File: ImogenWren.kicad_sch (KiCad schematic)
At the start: 16 parts, among them J1 Battery Cell 4.2v, J3 WS2821b-LED-Out, SW1 SW_SPDT_small, U1 MCP73831-2-OT

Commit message: dfhdyhdre
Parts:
- J3: value WS2821b-LED-Out -> WS2821b; PIN1 (none) -> gnd; PIN1_NAME D -> (none); PIN2 (none) -> V+; PIN2_NAME V+ -> (none); PIN3 (none) -> D; PIN3_NAME G -> (none)
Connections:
- net GND: now also J3.A1; no longer J3.A3
- net at JP3.2 (C): now also J3.A3; no longer J3.A1
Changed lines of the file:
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@@
     )
   )
-  (symbol (lib_id "000-edge-connectors-immo:3-pin-edge-touch") (at 259.08 92.71 0) (unit 1)
+  (symbol (lib_id "000-edge-connectors-immo:3-pin-edge-touch") (at 260.35 80.01 0) (mirror x) (unit 1)
     (in_bom yes) (on_board yes) (dnp no)
-    (property "Reference" "J3" (at 255.905 72.39 0)
+    (property "Reference" "J3" (at 250.19 87.63 0)
       (effects (font (size 1.27 1.27)) (justify left))
     )
-    (property "Value" "WS2821b-LED-Out" (at 255.27 74.295 0)
+    (property "Value" "WS2821b" (at 249.555 85.725 0)
       (effects (font (size 1.27 1.27)) (justify left))
     )
-    (property "Footprint" "000-edge-connectors-immo:3-pin-edge" (at 243.84 132.08 0)
+    (property "Footprint" "000-edge-connectors-immo:3-pin-edge" (at 297.18 86.36 0)
       (effects (font (size 1.27 1.27)) hide)
     )
-    (property "Datasheet" "http://www.ritrontek.com/uploadfile/2016/1026/20161026105231124.pdf#page=63" (at 262.89 120.65 0)
+    (property "Datasheet" "http://www.ritrontek.com/uploadfile/2016/1026/20161026105231124.pdf#page=63" (at 316.23 97.79 0)
       (effects (font (size 1.27 1.27)) hide)
     )
-    (property "PIN1_NAME" "D" (at 265.43 78.74 0)
+    (property "PIN1" "gnd" (at 266.7 81.28 0)
       (effects (font (size 1.27 1.27)))
     )
-    (property "PIN2_NAME" "V+" (at 266.7 81.28 0)
+    (property "PIN2" "V+" (at 266.065 80.01 0)
       (effects (font (size 1.27 1.27)))
     )
-    (property "PIN3_NAME" "G" (at 265.43 82.55 0)
+    (property "PIN3" "D" (at 265.43 77.47 0)
       (effects (font (size 1.27 1.27)))
     )

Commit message: Got to Routing. Keeps crashing on me
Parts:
- J1: value Battery Cell 4.2v -> LiPo_4v2
- JP2: value Power Routing -> usb/batt
- JP3: value LED_DATA_SOURCE -> led-data
- JPw1: value Disable Onboard LEDs -> led-pwr
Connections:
- net GNDPWR is gone; now on net GND: J1.A1, JP1.2 (C), R1.2, U1.2 (V_{SS})
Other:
- sheet ESP32 ports: added CHARGE_INHIBIT; removed none
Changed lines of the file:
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@@
+    (stroke (width 0) (type default))
+  )
+  (wire (pts (xy 29.845 78.105) (xy 29.845 75.565))
     (stroke (width 0) (type default))
   )
@@
     (stroke (width 0) (type default))
   )
+  (wire (pts (xy 29.845 75.565) (xy 23.495 75.565))
+    (stroke (width 0) (type default))
+  )
   (wire (pts (xy 123.19 39.37) (xy 123.19 40.64))
     (stroke (width 0) (type default))
@@
   )
   (wire (pts (xy 68.58 110.49) (xy 68.58 121.92))
+    (stroke (width 0) (type default))
+  )
+  (wire (pts (xy 23.495 75.565) (xy 23.495 78.105))
     (stroke (width 0) (type default))
   )
@@
     )
   )
+  (symbol (lib_id "power:GND") (at 29.845 78.105 0) (unit 1)
+    (in_bom yes) (on_board yes) (dnp no) (fields_autoplaced)
+    (property "Reference" "#PWR09" (at 29.845 84.455 0)
+      (effects (font (size 1.27 1.27)) hide)
+    )
+    (property "Value" "GND" (at 29.845 83.185 0)
+      (effects (font (size 1.27 1.27)))
+    )
+    (property "Footprint" "" (at 29.845 78.105 0)
+      (effects (font (size 1.27 1.27)) hide)
+    )
+    (property "Datasheet" "" (at 29.845 78.105 0)
+      (effects (font (size 1.27 1.27)) hide)
+    )
+    (pin "1")
+    (instances
+      (project "ImogenWren"
+        (path "/84b7ad53-68b5-40da-9777-f5bb9a09ecb4"
+          (reference "#PWR09") (unit 1)
+        )
+      )
+    )
+  )
   (symbol (lib_id "000_Connectors_Immo:Jumper_3_Bridged12") (at 109.22 39.37 90) (mirror x) (unit 1)
     (in_bom yes) (on_board yes) (dnp no)
@@
       (effects (font (size 1.27 1.27)) (justify left))
     )
-    (property "Value" "Power Routing" (at 107.95 37.465 90)
+    (property "Value" "usb/batt" (at 107.95 37.465 90)
       (effects (font (size 1.27 1.27)) (justify left))
     )
@@
       (effects (font (size 1.27 1.27)))
     )
-    (property "Value" "Disable Onboard LEDs" (at 201.2725 29.21 0)
+    (property "Value" "led-pwr" (at 201.2725 29.21 0)
       (effects (font (size 1.27 1.27)))
     )
@@
       (effects (font (size 1.27 1.27)))
     )
-    (property "Value" "LED_DATA_SOURCE" (at 229.87 72.39 0)
+    (property "Value" "led-data" (at 229.87 72.39 0)
       (effects (font (size 1.27 1.27)))
     )
@@
     )
   )
+  (symbol (lib_id "power:GNDPWR") (at 23.495 78.105 0) (unit 1)
+    (in_bom yes) (on_board yes) (dnp no) (fields_autoplaced)
+    (property "Reference" "#PWR08" (at 23.495 83.185 0)
+      (effects (font (size 1.27 1.27)) hide)
+    )
+    (property "Value" "GNDPWR" (at 23.368 83.185 0)
+      (effects (font (size 1.27 1.27)))
+    )
+    (property "Footprint" "" (at 23.495 79.375 0)
+      (effects (font (size 1.27 1.27)) hide)
+    )
+    (property "Datasheet" "" (at 23.495 79.375 0)
+      (effects (font (size 1.27 1.27)) hide)
+    )
+    (pin "1")
+    (instances
+      (project "ImogenWren"
+        (path "/84b7ad53-68b5-40da-9777-f5bb9a09ecb4"
+          (reference "#PWR08") (unit 1)
+        )
+      )
+    )
+  )
   (symbol (lib_id "power:GNDPWR") (at 91.44 135.89 0) (unit 1)
     (in_bom yes) (on_board yes) (dnp no) (fields_autoplaced)
@@
       (effects (font (size 1.27 1.27)) (justify left))
     )
-    (property "Value" "Battery Cell 4.2v" (at 131.445 102.235 0)
+    (property "Value" "LiPo_4v2" (at 135.89 102.235 0)
       (effects (font (size 1.27 1.27)) (justify left))
     )
@@
       (effects (font (size 1.27 1.27)) (justify right))
     )
+    (pin "CHARGE_INHIBIT" output (at 163.83 61.595 0)
+      (effects (font (size 1.27 1.27)) (justify right))
+    )

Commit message: Recoverd
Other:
- sheet ESP32 ports: added CHARGE_STATUS; removed none
- moved on the sheet: J1, JP1, R1, R2, R3, R4, R5, SW1, U1

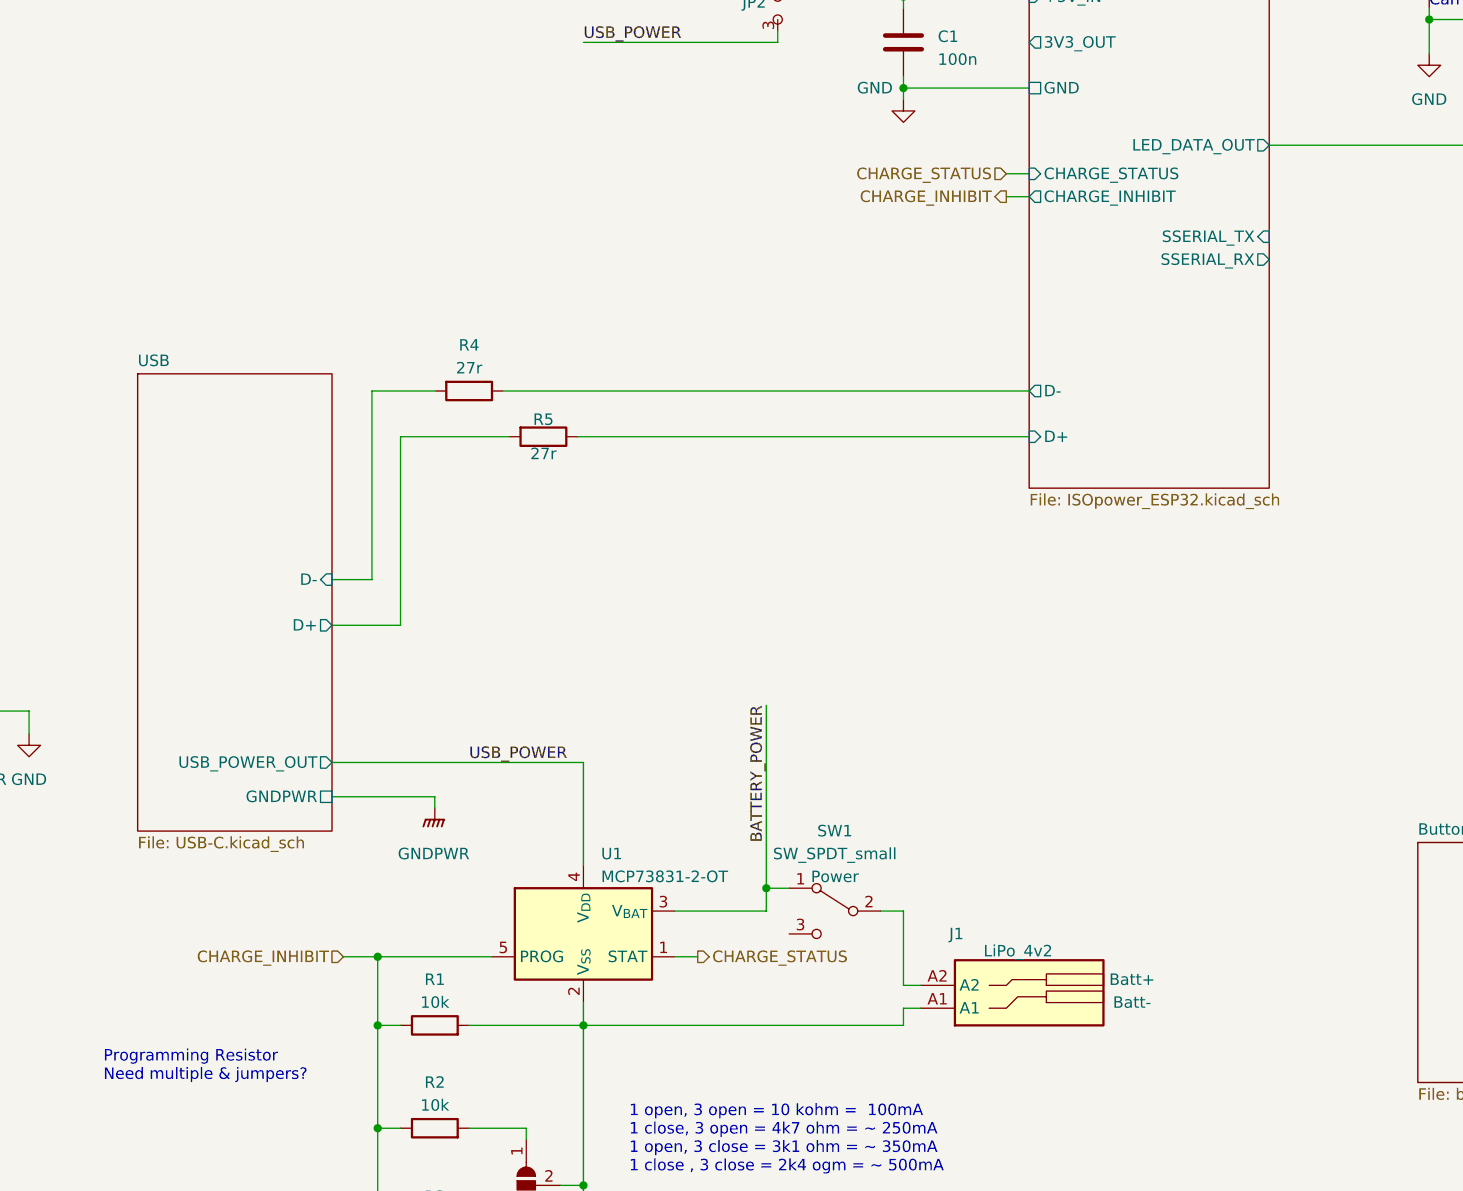
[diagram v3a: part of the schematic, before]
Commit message: Updated Schematic for Battery Charge Sense + read datasheet for battery charger IC
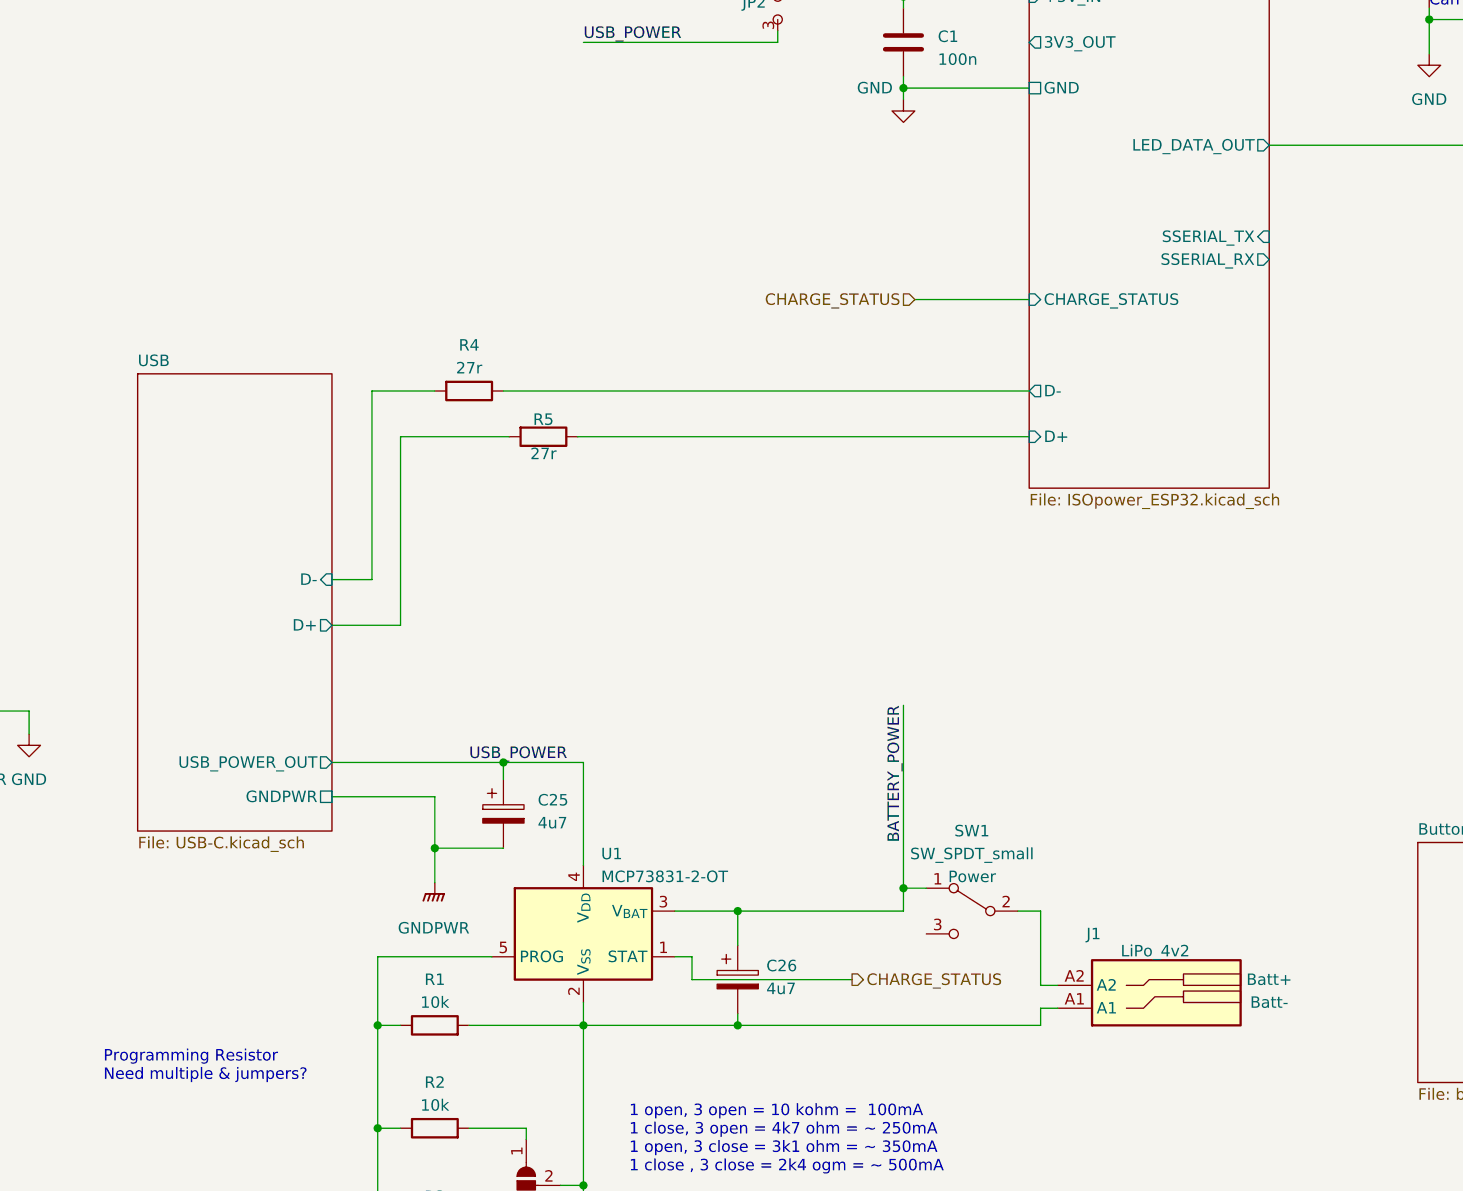
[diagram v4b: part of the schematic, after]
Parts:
- added C25, C26: 4u7, Capacitor_Tantalum_SMD:CP_EIA-2012-12_Kemet-R_Pad1.30x1.05mm_HandSolder, symbol 000_Capacitor_Film_Immo:tantalum
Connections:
- net BATTERY_POWER: now also C26.1
- net GND: now also C25.2, C26.2
- net USB_POWER: now also C25.1
- net CHARGE_INHIBIT: no longer names the net of R1.1, R2.1, R3.1, U1.5 (PROG)
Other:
- sheet ESP32 ports: added none; removed CHARGE_INHIBIT
- moved on the sheet: J1, SW1
